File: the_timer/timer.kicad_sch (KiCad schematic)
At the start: 19 parts, among them J1 AVR-ISP-6, J2 Conn_01x04_Socket, Q1 2N7002, Q2 2N7002, Q3 2N7002, U1 ATtiny48-A, U2 TPS61033, U3 MC3416, U4 W25Q128JVS, U5 MS5607-02BA

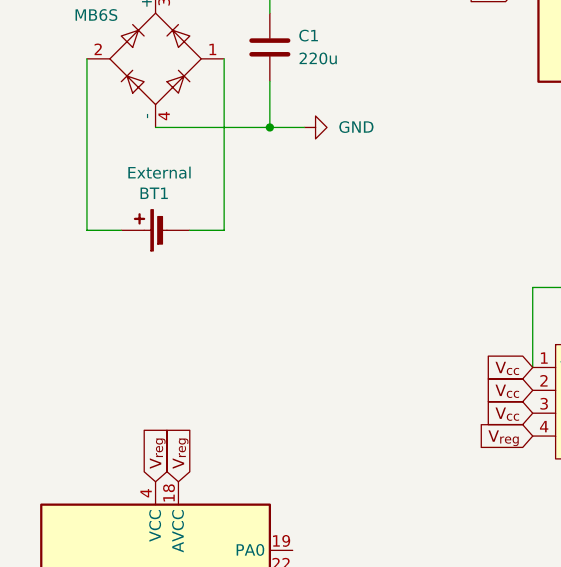
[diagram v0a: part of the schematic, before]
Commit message: added second battery terminal
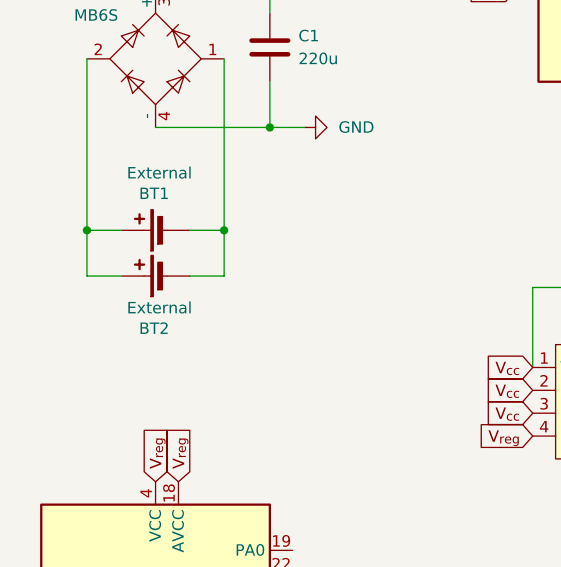
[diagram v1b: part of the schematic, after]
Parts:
- added BT2: External, locals:TE Right Angle JST, symbol Device:Battery_Cell
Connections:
- net at BT1.2 (-), D1.1: now also BT2.2 (-)
- net at BT1.1 (+), D1.2: now also BT2.1 (+)
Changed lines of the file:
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@@
+	)
+	(junction
+		(at 27.94 57.15)
+		(diameter 0)
+		(color 0 0 0 0)
+	)
+	(junction
+		(at 43.18 57.15)
+		(diameter 0)
+		(color 0 0 0 0)
 	)
 	(junction
@@
 	(wire
 		(pts
+			(xy 39.37 62.23) (xy 43.18 62.23)
+		)
+		(stroke
+			(width 0)
+			(type default)
+		)
+	)
+	(wire
+		(pts
 			(xy 97.79 80.01) (xy 107.95 80.01)
 		)
@@
 	(wire
 		(pts
+			(xy 31.75 62.23) (xy 27.94 62.23)
+		)
+		(stroke
+			(width 0)
+			(type default)
+		)
+	)
+	(wire
+		(pts
 			(xy 39.37 57.15) (xy 43.18 57.15)
 		)
@@
 		(pts
 			(xy 107.95 81.28) (xy 107.95 80.01)
+		)
+		(stroke
+			(width 0)
+			(type default)
+		)
+	)
+	(wire
+		(pts
+			(xy 27.94 62.23) (xy 27.94 57.15)
+		)
+		(stroke
+			(width 0)
+			(type default)
+		)
+	)
+	(wire
+		(pts
+			(xy 43.18 57.15) (xy 43.18 62.23)
 		)
 		(stroke
@@
 					(unit 1)
 				)
+			)
+		)
+	)
+	(symbol
+		(lib_id "Device:Battery_Cell")
+		(at 36.83 62.23 90)
+		(unit 1)
+		(exclude_from_sim no)
+		(in_bom yes)
+		(on_board yes)
+		(dnp no)
+		(property "Reference" "BT2"
+			(at 37.084 68.072 90)
+			(effects
+				(font
+					(size 1.27 1.27)
+				)
+				(justify left)
+			)
+		)
+		(property "Value" "External"
+			(at 39.624 65.786 90)
+			(effects
+				(font
+					(size 1.27 1.27)
+				)
+				(justify left)
+			)
+		)
+		(property "Footprint" "locals:TE Right Angle JST"
+			(at 35.306 62.23 90)
+			(effects
+				(font
+					(size 1.27 1.27)
+				)
+				(hide yes)
+			)
+		)
+		(property "Datasheet" "~"
+			(at 35.306 62.23 90)
+			(effects
+				(font
+					(size 1.27 1.27)
+				)
+				(hide yes)
+			)
+		)
+		(property "Description" ""
+			(at 36.83 62.23 0)
+			(effects
+				(font
+					(size 1.27 1.27)
+				)
+				(hide yes)
+			)
+		)
+		(property "DKPN" "A100080CT-ND"
+			(at 36.83 62.23 0)
+			(effects
+				(font
+					(size 1.27 1.27)
+				)
+				(hide yes)
+			)
+		)
+		(property "Field5" ""
+			(at 36.83 62.23 0)
+			(effects
+				(font
+					(size 1.27 1.27)
+				)
+				(hide yes)
+			)
+		)
+		(pin "1"
+		)
+		(pin "2"
+		)
+		(instances
+			(project "timer"
+				(path "/e2b0a296-fcac-4dcc-93f1-26b3dc1147d1"
+					(reference "BT2")
+					(unit 1)
+				)

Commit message: hell hell hell hell hell hell hell hell hell
updated timer to have a better layout and header pins. This layout is NOT yet screamer compatible and is not final
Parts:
- removed BT2: External, locals:TE Right Angle JST, symbol Device:Battery_Cell
- added J3: Conn_01x02_Socket, Connector_PinSocket_2.00mm:PinSocket_1x02_P2.00mm_Vertical, symbol Connector:Conn_01x02_Socket
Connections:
- net VB+: now reaches BT1.1 (+), D1.2
- net VB+: now also J3.2 (Pin_2)
- net VB-: now reaches BT1.2 (-), D1.1
- net VB-: now also J3.1 (Pin_1)
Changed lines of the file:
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@@
 	(title_block
 		(title "Timer")
-		(date "2024-04-12")
-		(rev "0.0.1")
+		(date "2024-04-16")
+		(rev "0.0.2")
 		(company "Mines Rocket Club")
 		(comment 1 "William Layne")
-	)
-	(junction
-		(at 27.94 57.15)
-		(diameter 0)
-		(color 0 0 0 0)
-	)
-	(junction
-		(at 43.18 57.15)
-		(diameter 0)
-		(color 0 0 0 0)
 	)
 	(junction
@@
 	(wire
 		(pts
-			(xy 39.37 62.23) (xy 43.18 62.23)
+			(xy 97.79 80.01) (xy 107.95 80.01)
 		)
 		(stroke
@@
 	(wire
 		(pts
-			(xy 97.79 80.01) (xy 107.95 80.01)
+			(xy 107.95 72.39) (xy 114.3 72.39)
 		)
 		(stroke
@@
 	(wire
 		(pts
-			(xy 107.95 72.39) (xy 114.3 72.39)
+			(xy 35.56 45.72) (xy 48.26 45.72)
 		)
 		(stroke
@@
 	(wire
 		(pts
-			(xy 35.56 45.72) (xy 48.26 45.72)
+			(xy 35.56 30.48) (xy 35.56 27.94)
 		)
 		(stroke
@@
 	(wire
 		(pts
-			(xy 35.56 30.48) (xy 35.56 27.94)
+			(xy 48.26 27.94) (xy 53.34 27.94)
 		)
 		(stroke
@@
 	(wire
 		(pts
-			(xy 48.26 27.94) (xy 53.34 27.94)
+			(xy 97.79 74.93) (xy 99.06 74.93)
 		)
 		(stroke
@@
 	(wire
 		(pts
-			(xy 97.79 74.93) (xy 99.06 74.93)
+			(xy 39.37 57.15) (xy 43.18 57.15)
 		)
 		(stroke
@@
 	(wire
 		(pts
-			(xy 31.75 62.23) (xy 27.94 62.23)
+			(xy 43.18 38.1) (xy 43.18 57.15)
 		)
 		(stroke
@@
 	(wire
 		(pts
-			(xy 39.37 57.15) (xy 43.18 57.15)
+			(xy 107.95 81.28) (xy 107.95 80.01)
 		)
 		(stroke
@@
 	(wire
 		(pts
-			(xy 43.18 38.1) (xy 43.18 57.15)
+			(xy 107.95 73.66) (xy 107.95 72.39)
 		)
 		(stroke
@@
 	(wire
 		(pts
-			(xy 107.95 81.28) (xy 107.95 80.01)
+			(xy 48.26 45.72) (xy 52.07 45.72)
 		)
 		(stroke
@@
 	(wire
 		(pts
-			(xy 27.94 62.23) (xy 27.94 57.15)
+			(xy 90.17 63.5) (xy 99.06 63.5)
 		)
 		(stroke
@@
 	(wire
 		(pts
-			(xy 43.18 57.15) (xy 43.18 62.23)
+			(xy 31.75 57.15) (xy 27.94 57.15)
 		)
 		(stroke
@@
 	(wire
 		(pts
-			(xy 107.95 73.66) (xy 107.95 72.39)
+			(xy 107.95 80.01) (xy 107.95 78.74)
 		)
 		(stroke
@@
 	(wire
 		(pts
-			(xy 48.26 45.72) (xy 52.07 45.72)
+			(xy 35.56 27.94) (xy 48.26 27.94)
 		)
 		(stroke
@@
 	(wire
 		(pts
-			(xy 90.17 63.5) (xy 99.06 63.5)
+			(xy 77.47 63.5) (xy 77.47 72.39)
 		)
 		(stroke
@@
 	(wire
 		(pts
-			(xy 31.75 57.15) (xy 27.94 57.15)
+			(xy 48.26 27.94) (xy 48.26 33.02)
 		)
 		(stroke
@@
 		)
 	)
-	(wire
-		(pts
-			(xy 107.95 80.01) (xy 107.95 78.74)
-		)
-		(stroke
-			(width 0)
-			(type default)
-		)
-	)
-	(wire
-		(pts
-			(xy 35.56 27.94) (xy 48.26 27.94)
-		)
-		(stroke
-			(width 0)
-			(type default)
-		)
-	)
-	(wire
-		(pts
-			(xy 77.47 63.5) (xy 77.47 72.39)
-		)
-		(stroke
-			(width 0)
-			(type default)
-		)
-	)
-	(wire
-		(pts
-			(xy 48.26 27.94) (xy 48.26 33.02)
-		)
-		(stroke
-			(width 0)
-			(type default)
-		)
-	)
 	(global_label "V_{reg}"
 		(shape input)
@@
 		)
 	)
+	(global_label "VB-"
+		(shape input)
+		(at 180.34 111.76 180)
+		(fields_autoplaced yes)
+		(effects
+			(font
+				(size 1.27 1.27)
+			)
+			(justify right)
+		)
+		(property "Intersheetrefs" "${INTERSHEET_REFS}"
+			(at 173.4238 111.76 0)
+			(effects
+				(font
+					(size 1.27 1.27)
+				)
+				(justify right)
+				(hide yes)
+			)
+		)
+	)
 	(global_label "c1"
 		(shape input)
@@
 		)
 	)
+	(global_label "VB+"
+		(shape input)
+		(at 27.94 57.15 180)
+		(fields_autoplaced yes)
+		(effects
+			(font
+				(size 1.27 1.27)
+			)
+			(justify right)
+		)
+		(property "Intersheetrefs" "${INTERSHEET_REFS}"
+			(at 21.0238 57.15 0)
+			(effects
+				(font
+					(size 1.27 1.27)
+				)
+				(justify right)
+				(hide yes)
+			)
+		)
+	)
 	(global_label "t0"
 		(shape input)
@@
 		(property "Intersheetrefs" "${INTERSHEET_REFS}"
 			(at 59.2064 27.94 0)
+			(effects
+				(font
+					(size 1.27 1.27)
+				)
+				(justify left)
+				(hide yes)
+			)
+		)
+	)
+	(global_label "VB+"
+		(shape input)
+		(at 180.34 114.3 180)
+		(fields_autoplaced yes)
+		(effects
+			(font
+				(size 1.27 1.27)
+			)
+			(justify right)
+		)
+		(property "Intersheetrefs" "${INTERSHEET_REFS}"
+			(at 173.4238 114.3 0)
+			(effects
+				(font
+					(size 1.27 1.27)
+				)
+				(justify right)
+				(hide yes)
+			)
+		)
+	)
+	(global_label "VB-"
+		(shape input)
+		(at 43.18 57.15 0)
+		(fields_autoplaced yes)
+		(effects
+			(font
+				(size 1.27 1.27)
+			)
+			(justify left)
+		)
+		(property "Intersheetrefs" "${INTERSHEET_REFS}"
+			(at 50.0962 57.15 0)
 			(effects
 				(font
@@
 	)
 	(symbol
+		(lib_id "Connector:Conn_01x02_Socket")
+		(at 185.42 111.76 0)
+		(unit 1)
+		(exclude_from_sim no)
+		(in_bom yes)
+		(on_board yes)
+		(dnp no)
+		(fields_autoplaced yes)
+		(property "Reference" "J3"
+			(at 186.69 111.7599 0)
+			(effects
+				(font
+					(size 1.27 1.27)
+				)
+				(justify left)
+			)
+		)
+		(property "Value" "Conn_01x02_Socket"
+			(at 186.69 114.2999 0)
+			(effects
+				(font
+					(size 1.27 1.27)
+				)
+				(justify left)
+			)
+		)
+		(property "Footprint" "Connector_PinSocket_2.00mm:PinSocket_1x02_P2.00mm_Vertical"
+			(at 185.42 111.76 0)
+			(effects
+				(font
+					(size 1.27 1.27)
+				)
+				(hide yes)
+			)
+		)
+		(property "Datasheet" "~"
+			(at 185.42 111.76 0)
+			(effects
+				(font
+					(size 1.27 1.27)
+				)
+				(hide yes)
+			)
+		)
+		(property "Description" "Generic connector, single row, 01x02, script generated"
+			(at 185.42 111.76 0)
+			(effects
+				(font
+					(size 1.27 1.27)
+				)
+				(hide yes)
+			)
+		)
+		(pin "1"
+		)
+		(pin "2"
+		)
+		(instances
+			(project "timer"
+				(path "/e2b0a296-fcac-4dcc-93f1-26b3dc1147d1"
+					(reference "J3")
+					(unit 1)
+				)
+			)
+		)
+	)
+	(symbol
 		(lib_id "Device:C")
 		(at 48.26 36.83 0)
@@
 					(unit 1)
 				)
-			)
-		)
-	)
-	(symbol
-		(lib_id "Device:Battery_Cell")
-		(at 36.83 62.23 90)
-		(unit 1)
-		(exclude_from_sim no)
-		(in_bom yes)
-		(on_board yes)
-		(dnp no)
-		(property "Reference" "BT2"
-			(at 37.084 68.072 90)
-			(effects
-				(font
-					(size 1.27 1.27)
-				)
-				(justify left)
-			)
-		)
-		(property "Value" "External"
-			(at 39.624 65.786 90)
-			(effects
-				(font
-					(size 1.27 1.27)
-				)
-				(justify left)
-			)
-		)
-		(property "Footprint" "locals:TE Right Angle JST"
-			(at 35.306 62.23 90)
-			(effects
-				(font
-					(size 1.27 1.27)
-				)
-				(hide yes)
-			)
-		)
-		(property "Datasheet" "~"
-			(at 35.306 62.23 90)
-			(effects
-				(font
-					(size 1.27 1.27)
-				)
-				(hide yes)
-			)
-		)
-		(property "Description" ""
-			(at 36.83 62.23 0)
-			(effects
-				(font
-					(size 1.27 1.27)
-				)
-				(hide yes)
-			)
-		)
-		(property "DKPN" "A100080CT-ND"
-			(at 36.83 62.23 0)
-			(effects
-				(font
-					(size 1.27 1.27)
-				)
-				(hide yes)
-			)
-		)
-		(property "Field5" ""
-			(at 36.83 62.23 0)
-			(effects
-				(font
-					(size 1.27 1.27)
-				)
-				(hide yes)
-			)
-		)
-		(pin "1"
-		)
-		(pin "2"
-		)
-		(instances
-			(project "timer"
-				(path "/e2b0a296-fcac-4dcc-93f1-26b3dc1147d1"
-					(reference "BT2")
-					(unit 1)
-				)
